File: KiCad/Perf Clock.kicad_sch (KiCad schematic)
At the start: 7 parts, among them U1 PIC16LF1826IP, U2 74HC595, U3 74HC595, U4 TLC5916IN, U5 TLC5916IN

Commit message: February Update
Made Progress on the Renderer
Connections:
- net SNK_CLK: no longer U1.11 (RB5)
- net SNK_LE: now also U1.16 (RA7); no longer U1.2 (RA3)
- net SNK_SDI: no longer U1.8 (RB2)
- net SRC_SRCLK: no longer U1.10 (RB4)
- net uC_SER: no longer U1.7 (RB1)
- net ~{SNK_OE}: now also U1.15 (RA6); no longer U1.3 (RA4)
- net ~{SRC_OE}: now also U1.17 (RA0); no longer U1.1 (RA2)
- net ~{SRC_SRCLR}: no longer U1.17 (RA0)
- new net USART_CLK: U1.8 (RB2)
- new net USART_DATA: U1.7 (RB1)
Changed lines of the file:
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@@
   (no_connect (at 139.7 123.19))
   (no_connect (at 185.42 91.44))
-  (no_connect (at 71.12 160.02))
   (no_connect (at 180.34 123.19))
   (no_connect (at 93.98 144.78))
   (no_connect (at 187.96 91.44))
+  (no_connect (at 93.98 154.94))
   (no_connect (at 182.88 91.44))
-  (no_connect (at 71.12 162.56))
   (no_connect (at 191.77 121.92))
+  (no_connect (at 93.98 157.48))
   (no_connect (at 93.98 152.4))
   (wire (pts (xy 152.4 38.1) (xy 162.56 38.1))
@@
     (stroke (width 0) (type default))
   )
+  (wire (pts (xy 59.69 144.78) (xy 71.12 144.78))
+    (stroke (width 0) (type default))
+  )
   (wire (pts (xy 191.77 111.76) (xy 191.77 121.92))
     (stroke (width 0) (type default))
@@
     (stroke (width 0) (type default))
   )
+  (wire (pts (xy 59.69 160.02) (xy 71.12 160.02))
+    (stroke (width 0) (type default))
+  )
   (wire (pts (xy 63.5 33.02) (xy 63.5 24.13))
     (stroke (width 0) (type default))
@@
     (stroke (width 0) (type default))
   )
-  (wire (pts (xy 93.98 157.48) (xy 105.41 157.48))
-    (stroke (width 0) (type default))
-  )
   (wire (pts (xy 152.4 45.72) (xy 162.56 45.72))
     (stroke (width 0) (type default))
@@
     (stroke (width 0) (type default))
   )
-  (wire (pts (xy 93.98 154.94) (xy 105.41 154.94))
-    (stroke (width 0) (type default))
-  )
   (wire (pts (xy 184.15 111.76) (xy 184.15 127))
     (stroke (width 0) (type default))
@@
     (stroke (width 0) (type default))
   )
+  (wire (pts (xy 59.69 162.56) (xy 71.12 162.56))
+    (stroke (width 0) (type default))
+  )
   (wire (pts (xy 190.5 43.18) (xy 190.5 44.45))
     (stroke (width 0) (type default))
@@
   )
   (wire (pts (xy 200.66 69.85) (xy 200.66 72.39))
-    (stroke (width 0) (type default))
-  )
-  (wire (pts (xy 59.69 144.78) (xy 71.12 144.78))
     (stroke (width 0) (type default))
   )
@@
     (effects (font (size 1.27 1.27)) (justify right bottom))
   )
-  (label "SNK_SDI" (at 105.41 149.86 180) (fields_autoplaced)
-    (effects (font (size 1.27 1.27)) (justify right bottom))
-  )
   (label "SNKCLK" (at 134.62 121.92 90) (fields_autoplaced)
     (effects (font (size 1.27 1.27)) (justify left bottom))
@@
     (effects (font (size 1.27 1.27)) (justify right bottom))
   )
-  (label "SNK_LE" (at 59.69 152.4 0) (fields_autoplaced)
-    (effects (font (size 1.27 1.27)) (justify left bottom))
-  )
   (label "SNK_SDO" (at 151.13 121.92 90) (fields_autoplaced)
     (effects (font (size 1.27 1.27)) (justify left bottom))
@@
     (effects (font (size 1.27 1.27)) (justify right bottom))
   )
+  (label "USART_CLK" (at 105.41 149.86 180) (fields_autoplaced)
+    (effects (font (size 1.27 1.27)) (justify right bottom))
+  )
   (label "SINK8" (at 113.03 72.39 270) (fields_autoplaced)
     (effects (font (size 1.27 1.27)) (justify right bottom))
@@
     (effects (font (size 1.27 1.27)) (justify left bottom))
   )
+  (label "~{SNK_OE}" (at 59.69 160.02 0) (fields_autoplaced)
+    (effects (font (size 1.27 1.27)) (justify left bottom))
+  )
   (label "SINK7" (at 107.95 72.39 270) (fields_autoplaced)
     (effects (font (size 1.27 1.27)) (justify right bottom))
@@
     (effects (font (size 1.27 1.27)) (justify left bottom))
   )
+  (label "~{SRC_OE}" (at 59.69 144.78 0) (fields_autoplaced)
+    (effects (font (size 1.27 1.27)) (justify left bottom))
+  )
   (label "SNK_SDI" (at 182.88 59.69 270) (fields_autoplaced)
     (effects (font (size 1.27 1.27)) (justify right bottom))
   )
-  (label "~{SNK_OE}" (at 59.69 154.94 0) (fields_autoplaced)
-    (effects (font (size 1.27 1.27)) (justify left bottom))
-  )
   (label "SNK_LE" (at 177.8 121.92 90) (fields_autoplaced)
     (effects (font (size 1.27 1.27)) (justify left bottom))
@@
     (effects (font (size 1.27 1.27)) (justify right bottom))
   )
-  (label "uC_SER" (at 105.41 147.32 180) (fields_autoplaced)
-    (effects (font (size 1.27 1.27)) (justify right bottom))
-  )
-  (label "SNK_CLK" (at 105.41 157.48 180) (fields_autoplaced)
+  (label "USART_DATA" (at 105.41 147.32 180) (fields_autoplaced)
     (effects (font (size 1.27 1.27)) (justify right bottom))
   )
@@
     (effects (font (size 1.27 1.27)) (justify left bottom))
   )
-  (label "~{SRC_OE}" (at 59.69 149.86 0) (fields_autoplaced)
+  (label "SNK_LE" (at 59.69 162.56 0) (fields_autoplaced)
     (effects (font (size 1.27 1.27)) (justify left bottom))
   )
@@
     (effects (font (size 1.27 1.27)) (justify left bottom))
   )
-  (label "~{SRC_SRCLR}" (at 59.69 144.78 0) (fields_autoplaced)
-    (effects (font (size 1.27 1.27)) (justify left bottom))
-  )
   (label "~{SNK_OE}" (at 146.05 121.92 90) (fields_autoplaced)
     (effects (font (size 1.27 1.27)) (justify left bottom))
@@
     (effects (font (size 1.27 1.27)) (justify right bottom))
   )
-  (label "SRC_SRCLK" (at 105.41 154.94 180) (fields_autoplaced)
-    (effects (font (size 1.27 1.27)) (justify right bottom))
-  )

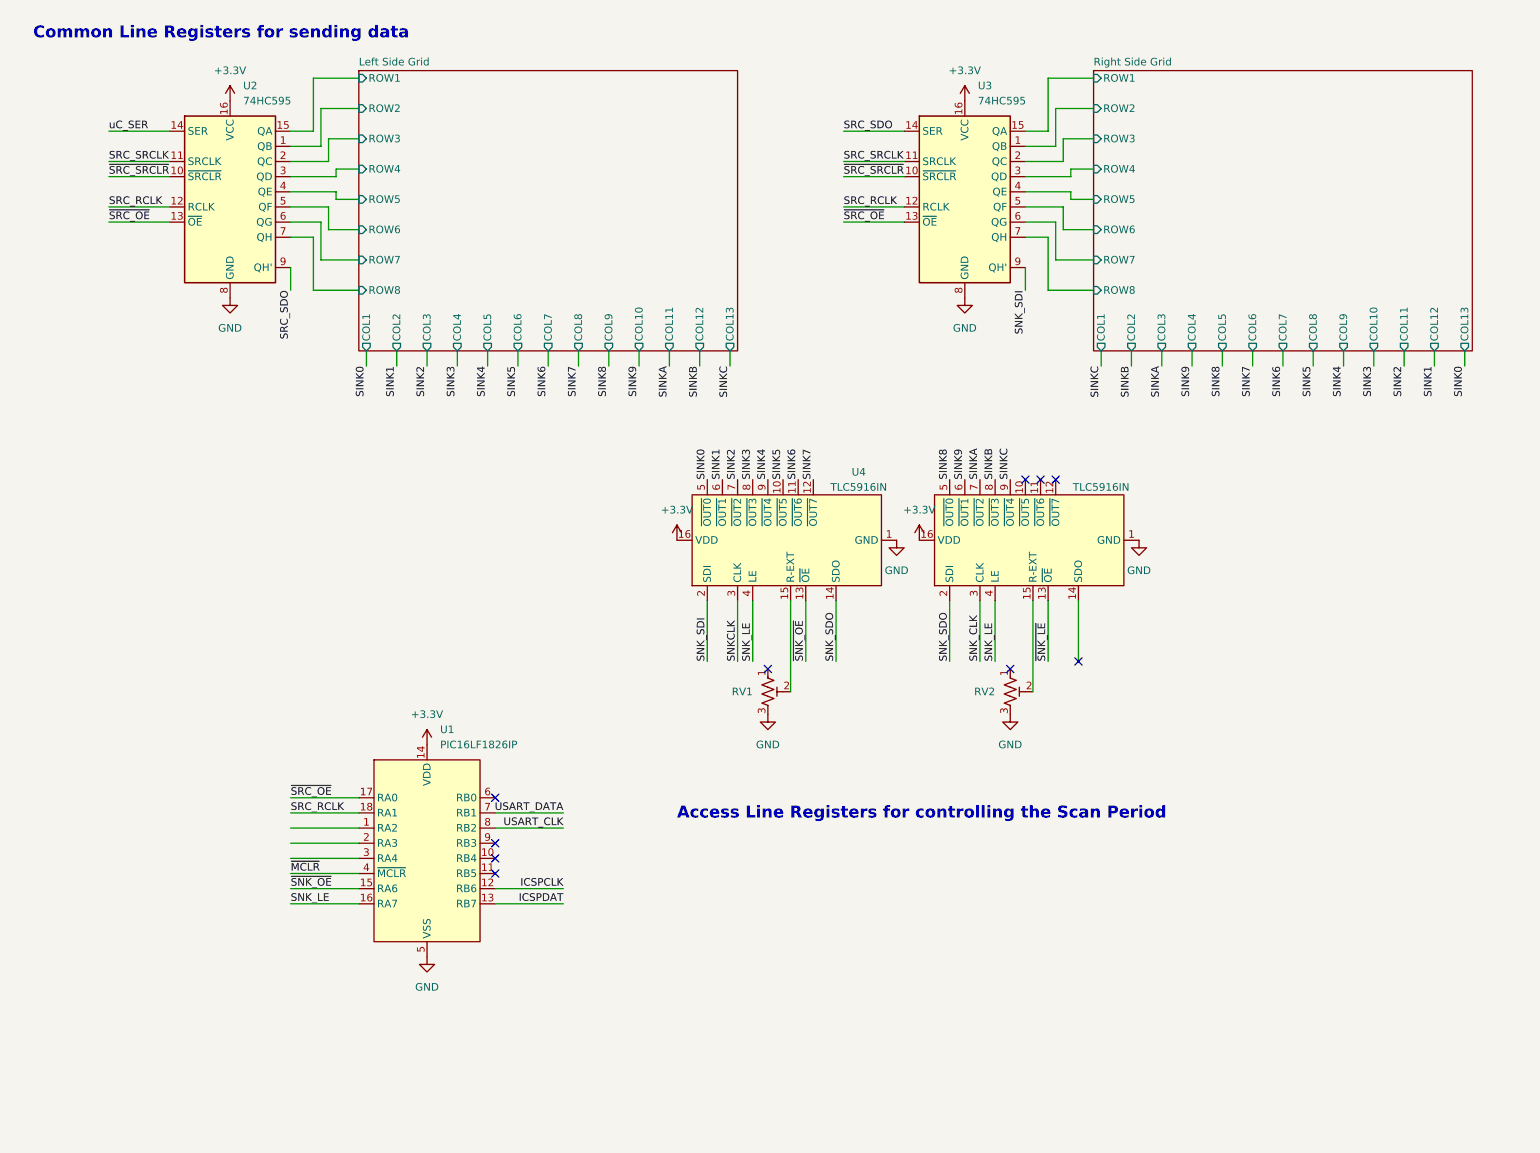
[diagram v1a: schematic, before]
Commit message: Perf Board Wiring
Finished wiring the Perf board
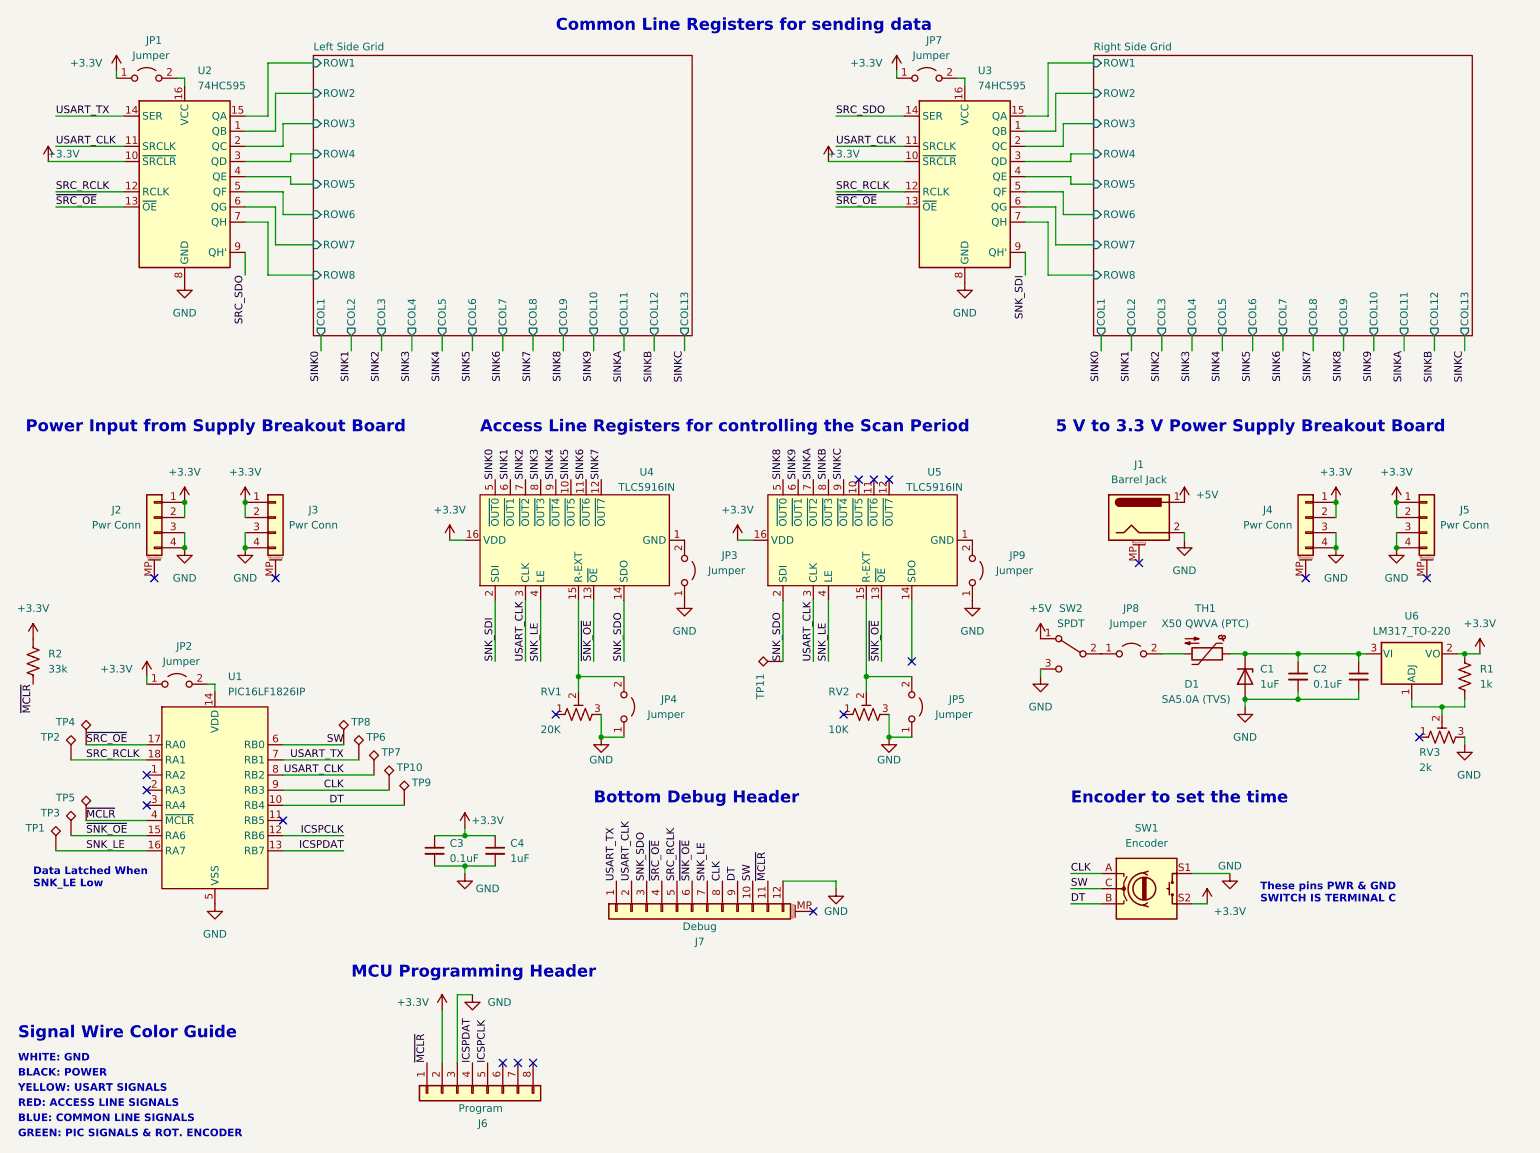
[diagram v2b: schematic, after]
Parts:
- added C1, C4: 1uF, symbol Device:C_Small
- added C2, C3: 0.1uF, symbol Device:C_Small
- added D1: SA5.0A (TVS), symbol Device:D_Zener
- added J1: Barrel Jack, symbol Connector:Barrel_Jack_MountingPin
- added J2, J3, J4, J5: Pwr Conn, symbol Connector_Generic_MountingPin:Conn_01x04_MountingPin
- added J6: Program, symbol Connector_Generic:Conn_01x08
- added J7: Debug, symbol Connector_Generic_MountingPin:Conn_01x12_MountingPin
- added JP1, JP2, JP3, JP4, JP5, JP7, JP8, JP9: Jumper, symbol Jumper:Jumper_2_Open
- added R1: 1k, symbol Device:R_US
- added R2: 33k, symbol Device:R_US
- added RV3: 2k, symbol Device:R_Potentiometer_Trim_US
- added SW1: Encoder, symbol Device:RotaryEncoder_Switch
- added SW2: SPDT, symbol Switch:SW_SPDT
- added TH1: X50 QWVA (PTC), symbol Device:Thermistor_NTC
- added TP1, TP10, TP11, TP2, TP3, TP4, TP5, TP6, TP7, TP8, TP9: ~, symbol Connector:TestPoint_Alt
- added U6: LM317_TO-220, Package_TO_SOT_THT:TO-220-3_Vertical, symbol Regulator_Linear:LM317_TO-220
- RV1: value ~ -> 20K
- RV2: value ~ -> 10K
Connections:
- net SNKCLK is gone; now on net USART_CLK: U4.3 (CLK)
- net SNK_CLK is gone; now on net USART_CLK: U5.3 (CLK)
- net SRC_SRCLK is gone; now on net USART_CLK: U2.11 (SRCLK), U3.11 (SRCLK)
- net uC_SER is gone; now on net USART_TX: U2.14 (SER)
- net ~{SNK_LE} is gone; now on net ~{SNK_OE}: U5.13 (~{OE})
- net ~{SRC_SRCLR} is gone; now on net +3.3V: U2.10 (~{SRCLR}), U3.10 (~{SRCLR})
- net +3.3V: now also C3.1, C4.1, J2.1 (Pin_1), J2.2 (Pin_2), J3.1 (Pin_1), J3.2 (Pin_2), J4.1 (Pin_1), J4.2 (Pin_2), J5.1 (Pin_1), J5.2 (Pin_2), J6.2 (Pin_2), JP1.1 (A), JP2.1 (A), JP7.1 (A), R1.1, R2.1, SW1.S2, U6.2 (VO); no longer U1.14 (VDD), U2.16 (VCC), U3.16 (VCC)
- net GND: now also C1.2, C2.2, C3.2, C4.2, D1.2 (A), J1.2, J2.3 (Pin_3), J2.4 (Pin_4), J3.3 (Pin_3), J3.4 (Pin_4), J4.3 (Pin_3), J4.4 (Pin_4), J5.3 (Pin_3), J5.4 (Pin_4), J6.3 (Pin_3), J7.12 (Pin_12), JP3.1 (A), JP4.1 (A), JP5.1 (A), JP9.1 (A), RV3.3, SW1.S1, SW2.3 (C); no longer U4.1 (GND), U5.1 (GND)
- net ICSPCLK: now also J6.5 (Pin_5)
- net ICSPDAT: now also J6.4 (Pin_4)
- net SNK_LE: now also J7.7 (Pin_7), TP1.1
- net SNK_SDO: now also J7.3 (Pin_3), TP11.1
- net SRC_RCLK: now also J7.5 (Pin_5), TP2.1
- net USART_CLK: now also J7.2 (Pin_2), TP7.1
- net ~{MCLR}: now also J6.1 (Pin_1), J7.11 (Pin_11), R2.2, TP5.1
- net ~{SNK_OE}: now also J7.6 (Pin_6), TP3.1
- net ~{SRC_OE}: now also J7.4 (Pin_4), TP4.1
- net at RV1.2, U4.15 (R-EXT): now also JP4.2 (B)
- net at RV2.2, U5.15 (R-EXT): now also JP5.2 (B)
- net DT: now reaches U1.10 (RB4)
- net DT: now also J7.9 (Pin_9), SW1.B, TP9.1
- net SW: now reaches U1.6 (RB0)
- net SW: now also J7.10 (Pin_10), SW1.C, TP8.1
- net CLK: now reaches U1.9 (RB3)
- net CLK: now also J7.8 (Pin_8), SW1.A, TP10.1
- net USART_DATA renamed USART_TX
- net USART_TX: now also J7.1 (Pin_1), TP6.1
- new net: R1.2, RV3.2, U6.1 (ADJ)
- new net: C1.1, C2.1, D1.1 (K), TH1.1, U6.3 (VI)
- new net: JP8.2 (B), TH1.2
- new net: JP8.1 (A), SW2.2 (B)
- new net: JP1.2 (B), U2.16 (VCC)
- new net: JP3.2 (B), U4.1 (GND)
- new net: JP9.2 (B), U5.1 (GND)
- new net: JP7.2 (B), U3.16 (VCC)
- new net: JP2.2 (B), U1.14 (VDD)
- new net +5V: J1.1, SW2.1 (A)
- no-connect marks 10 -> 20
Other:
- note added: "5 V to 3.3 V Power Supply Breakout Board"
- note added: "BLACK: POWER"
- note added: "BLUE: COMMON LINE SIGNALS"
- note added: "Bottom Debug Header"
- note added: "Data Latched When SNK_LE Low"
- note added: "Encoder to set the time"
- note added: "GREEN: PIC SIGNALS & ROT. ENCODER"
- note added: "MCU Programming Header"
- note added: "Power Input from Supply Breakout Board"
- note added: "RED: ACCESS LINE SIGNALS"
- note added: "Signal Wire Color Guide"
- note added: "These pins PWR & GND SWITCH IS TERMINAL C"
- note added: "WHITE: GND"
- note added: "YELLOW: USART SIGNALS"
- title: Perf Board Clock -> Gator Clock
- moved on the sheet: RV1, RV2, U1, U2, U3, U4
